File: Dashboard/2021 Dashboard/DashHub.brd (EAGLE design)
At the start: 86.4 x 66 mm, 26 parts, among them J1 LEFT, J2 RIGHT, U1 ALLEGRO_MICROSYSTEMS_ACS722LL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

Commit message: Linear Regulator
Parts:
- removed U$3: DC-DC-STEP-DOWN-MP1584, diy-modules:DC-DC-STEP-DOWN-MP1584
- added C3: 10uF, GTOR - Passive Components:C1206
- added C5, C6: 47uF, GTOR - Passive Components:C1206
- added U$6: TPSM84205EAB, GTOR - Active Components:TPSM84205EAB
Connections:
- removed net 3.3V_BUCK: J1.08, J2.08, U$3.OUT+.1, U$3.OUT+.2
- new net 3.3V_REG: C5.1, C6.1, J1.08, J2.08, U$6.3
- net 7.4V: now also C3.2, U$6.1; no longer U$3.IN+.1, U$3.IN+.2
- net GND: now also U$6.2; no longer U$3.IN-.1, U$3.IN-.2, U$3.OUT-.1, U$3.OUT-.2
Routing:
- net 3.3V_BUCK: track 75.9 -> 0.00 mm, vias 2 -> 0
- net 3.3V_REG: track 0.00 -> 68.9 mm, vias 0 -> 2
- net GND: track 336.4 -> 302.4 mm
- net 7.4V: track 158.7 -> 149.0 mm
- added copper zone on layer 1, net 3.3V_REG
- removed copper zone on layer 1, net 3.3V_BUCK
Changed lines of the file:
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@@
 <attribute name="VALUE" x="38.481" y="20.32" size="1.27" layer="27" rot="R90" align="top-center"/>
-</element>
-<element name="U$3" library="diy-modules" package="DC-DC-STEP-DOWN-MP1584" value="DC-DC-STEP-DOWN-MP1584" x="-33.02" y="-11.176" smashed="yes" rot="R90">
-<attribute name="NAME" x="-42.037" y="-11.176" size="1.27" layer="26" rot="MR270" align="bottom-center"/>
-<attribute name="VALUE" x="-23.495" y="-11.176" size="1.27" layer="27" rot="R90" align="top-center"/>
 </element>
 <element name="U$4" library="GTOR - Connectors" package="48CKTRASCMCHEADER" value="48CKTRASCMCHEADER" x="-10.16" y="23.368" smashed="yes" rot="MR0"/>
 <element name="U$5" library="GTOR - Breakout Boards" package="DIYMALL_6M_GPS_BREAKOUT" value="DIYMALL_6M_GPS_BREAKOUT" x="75.692" y="24.384" smashed="yes" rot="R179.9"/>
+<element name="U$6" library="GTOR - Active Components" package="TPSM84205EAB" value="TPSM84205EAB" x="-67.056" y="-27.94" smashed="yes">
+<attribute name="NAME" x="-72.136" y="-24.13" size="1.27" layer="25"/>
+<attribute name="VALUE" x="-72.136" y="-33.655" size="1.27" layer="27"/>
+</element>
+<element name="C3" library="GTOR - Passive Components" package="C1206" package3d_urn="urn:adsk.eagle:package:23618/2" value="10uF" x="-70.104" y="-42.164" smashed="yes">
+<attribute name="NAME" x="-71.374" y="-40.894" size="1.27" layer="25"/>
+<attribute name="POPULARITY" value="54" x="-70.104" y="-42.164" size="1.778" layer="27" display="off"/>
+<attribute name="SPICEPREFIX" value="C" x="-70.104" y="-42.164" size="1.778" layer="27" display="off"/>
+<attribute name="VALUE" x="-71.374" y="-44.704" size="1.27" layer="27"/>
+</element>
+<element name="C5" library="GTOR - Passive Components" package="C1206" package3d_urn="urn:adsk.eagle:package:23618/2" value="47uF" x="-70.104" y="-51.308" smashed="yes">
+<attribute name="NAME" x="-71.374" y="-50.038" size="1.27" layer="25"/>
+<attribute name="POPULARITY" value="54" x="-70.104" y="-51.308" size="1.778" layer="27" display="off"/>
+<attribute name="SPICEPREFIX" value="C" x="-70.104" y="-51.308" size="1.778" layer="27" display="off"/>
+<attribute name="VALUE" x="-71.374" y="-53.848" size="1.27" layer="27"/>
+</element>
+<element name="C6" library="GTOR - Passive Components" package="C1206" package3d_urn="urn:adsk.eagle:package:23618/2" value="47uF" x="-70.104" y="-55.88" smashed="yes">
+<attribute name="NAME" x="-71.374" y="-54.61" size="1.27" layer="25"/>
+<attribute name="POPULARITY" value="54" x="-70.104" y="-55.88" size="1.778" layer="27" display="off"/>
+<attribute name="SPICEPREFIX" value="C" x="-70.104" y="-55.88" size="1.778" layer="27" display="off"/>
+<attribute name="VALUE" x="-71.374" y="-58.42" size="1.27" layer="27"/>
+</element>
 </elements>
 <signals>
@@
 <contactref element="U$2" pad="OUT-.1"/>
 <contactref element="U$2" pad="OUT-.2"/>
-<contactref element="U$3" pad="IN-.1"/>
-<contactref element="U$3" pad="IN-.2"/>
-<contactref element="U$3" pad="OUT-.1"/>
-<contactref element="U$3" pad="OUT-.2"/>
-<wire x1="-37.084" y1="-20.447" x2="-33.655" y2="-23.876" width="0.4064" layer="1"/>
 <wire x1="-33.655" y1="-23.876" x2="-24.892" y2="-23.876" width="0.4064" layer="1"/>
 <wire x1="-24.892" y1="-23.876" x2="-17.4498" y2="-16.4338" width="0.4064" layer="1"/>
@@
 <wire x1="38.608" y1="-19.812" x2="37.0538" y2="-19.812" width="0.1524" layer="1"/>
 <wire x1="37.0538" y1="-19.812" x2="36.6794" y2="-19.4376" width="0.1524" layer="1"/>
-<wire x1="-37.084" y1="-20.447" x2="-39.624" y2="-20.447" width="0.1524" layer="1"/>
-<wire x1="-39.624" y1="-20.447" x2="-39.584" y2="-20.487" width="0.1524" layer="1"/>
 <wire x1="-39.584" y1="-20.487" x2="-39.584" y2="-27.813" width="0.1524" layer="1"/>
 <wire x1="-27.178" y1="-30.613" x2="-27.8944" y2="-29.8966" width="0.1524" layer="16"/>
@@
 <wire x1="-27.8944" y1="-29.6433125" x2="-28.3785125" y2="-29.1592" width="0.1524" layer="16"/>
 <wire x1="-28.3785125" y1="-29.1592" x2="-31.62225625" y2="-29.1592" width="0.1524" layer="16"/>
-<wire x1="-39.624" y1="-20.447" x2="-39.624" y2="-2.032" width="0.1524" layer="1"/>
-<wire x1="-39.624" y1="-2.032" x2="-39.624" y2="-1.905" width="0.1524" layer="1"/>
-<wire x1="-37.084" y1="-1.905" x2="-37.211" y2="-2.032" width="0.1524" layer="1"/>
-<wire x1="-37.211" y1="-2.032" x2="-39.624" y2="-2.032" width="0.1524" layer="1"/>
-<wire x1="-39.624" y1="-1.905" x2="-39.624" y2="3.556" width="0.1524" layer="16"/>
 <wire x1="-39.624" y1="3.556" x2="-35.56" y2="7.62" width="0.1524" layer="16"/>
 <wire x1="-35.56" y1="7.62" x2="-35.56" y2="9.525" width="0.1524" layer="16"/>
@@
 <wire x1="37.084" y1="0" x2="16.51" y2="0" width="0.1524" layer="1"/>
 <wire x1="11.43" y1="5.08" x2="16.51" y2="0" width="0.1524" layer="1"/>
-<wire x1="36.6794" y1="-19.4376" x2="74.16810625" y2="10.6966375" width="0" layer="19" extent="1-1"/>
+<contactref element="U$6" pad="2"/>
+<wire x1="-39.584" y1="-27.813" x2="-67.056" y2="-27.94" width="0" layer="19" extent="1-1"/>
+<wire x1="-33.655" y1="-23.876" x2="-39.584" y2="-20.487" width="0" layer="19" extent="1-1"/>
+<wire x1="-39.624" y1="3.556" x2="-39.584" y2="-20.487" width="0" layer="19" extent="1-16"/>
+<wire x1="74.16810625" y1="10.6966375" x2="36.6794" y2="-19.4376" width="0" layer="19" extent="1-1"/>
 </signal>
 <signal name="LAT_L">
@@
 <contactref element="U$2" pad="IN+.1"/>
 <contactref element="U$2" pad="IN+.2"/>
-<contactref element="U$3" pad="IN+.1"/>
-<contactref element="U$3" pad="IN+.2"/>
-<wire x1="-26.416" y1="-20.447" x2="-28.956" y2="-20.447" width="0.4064" layer="16"/>
-<wire x1="-26.416" y1="-20.447" x2="-22.733" y2="-16.764" width="0.4064" layer="1"/>
 <wire x1="-22.733" y1="-16.764" x2="-19.304" y2="-16.764" width="0.4064" layer="1"/>
 <wire x1="-19.304" y1="-16.764" x2="-18.796" y2="-16.256" width="0.4064" layer="1"/>
@@
 <wire x1="-28.448" y1="-25.013" x2="-28.448" y2="-22.86" width="0.4064" layer="16"/>
 <wire x1="-28.448" y1="-22.86" x2="-28.956" y2="-22.352" width="0.4064" layer="16"/>
-<wire x1="-28.956" y1="-22.352" x2="-28.956" y2="-20.447" width="0.4064" layer="16"/>
 <wire x1="39.116" y1="7.493" x2="35.56" y2="11.049" width="0.4064" layer="16"/>
 <wire x1="39.116" y1="-22.352" x2="39.116" y2="7.493" width="0.4064" layer="16"/>
 <wire x1="35.56" y1="11.049" x2="33.02" y2="11.049" width="0.4064" layer="16"/>
+<contactref element="U$6" pad="1"/>
+<contactref element="C3" pad="2"/>
+<wire x1="-69.596" y1="-27.94" x2="-68.704" y2="-42.164" width="0" layer="19" extent="1-1"/>
+<wire x1="-28.956" y1="-22.352" x2="-69.596" y2="-27.94" width="0" layer="19" extent="16-16"/>
+<wire x1="-27.178" y1="-25.013" x2="-28.448" y2="-25.013" width="0" layer="19" extent="16-16"/>
+<wire x1="-22.733" y1="-16.764" x2="-28.956" y2="-22.352" width="0" layer="19" extent="1-16"/>
 </signal>
 <signal name="3.3V_TEENSY">
@@
 <wire x1="6.1084" y1="19.812" x2="1.536" y2="19.812" width="0.1524" layer="16"/>
 </signal>
-<signal name="3.3V_BUCK">
+<signal name="3.3V_REG">
 <contactref element="J1" pad="08"/>
 <polygon width="0.1524" layer="1">
@@
 <wire x1="-21.59" y1="-11.43" x2="-19.57761875" y2="-11.43" width="0.4064" layer="16"/>
 <contactref element="J2" pad="08"/>
-<contactref element="U$3" pad="OUT+.1"/>
-<contactref element="U$3" pad="OUT+.2"/>
-<wire x1="-26.416" y1="-1.905" x2="-28.956" y2="-1.905" width="0.3048" layer="16"/>
 <wire x1="-21.971" y1="-5.842" x2="-25.908" y2="-1.905" width="0.4064" layer="16"/>
-<wire x1="-25.908" y1="-1.905" x2="-26.416" y2="-1.905" width="0.4064" layer="16"/>
 <wire x1="14.269075" y1="-4.4282" x2="13.904875" y2="-4.064" width="0.1524" layer="1"/>
 <wire x1="13.904875" y1="-4.064" x2="9.652" y2="-4.064" width="0.1524" layer="1"/>
@@
 <wire x1="-9.493" y1="0.508" x2="-9.775075" y2="0.508" width="0.1524" layer="16"/>
 <via x="-26.416" y="2.032" extent="1-16" drill="0.35"/>
-<wire x1="-26.416" y1="2.032" x2="-26.416" y2="-1.905" width="0.1524" layer="1"/>
+<contactref element="U$6" pad="3"/>
+<contactref element="C5" pad="1"/>
+<contactref element="C6" pad="1"/>
+<wire x1="-71.504" y1="-51.308" x2="-71.504" y2="-55.88" width="0" layer="19" extent="1-1"/>
+<wire x1="-64.516" y1="-27.94" x2="-71.504" y2="-51.308" width="0" layer="19" extent="1-1"/>
+<wire x1="-25.908" y1="-1.905" x2="-64.516" y2="-27.94" width="0" layer="19" extent="16-16"/>
+<wire x1="-26.416" y1="2.032" x2="-25.908" y2="-1.905" width="0" layer="19" extent="16-16"/>
 </signal>
 <signal name="LAT_D">

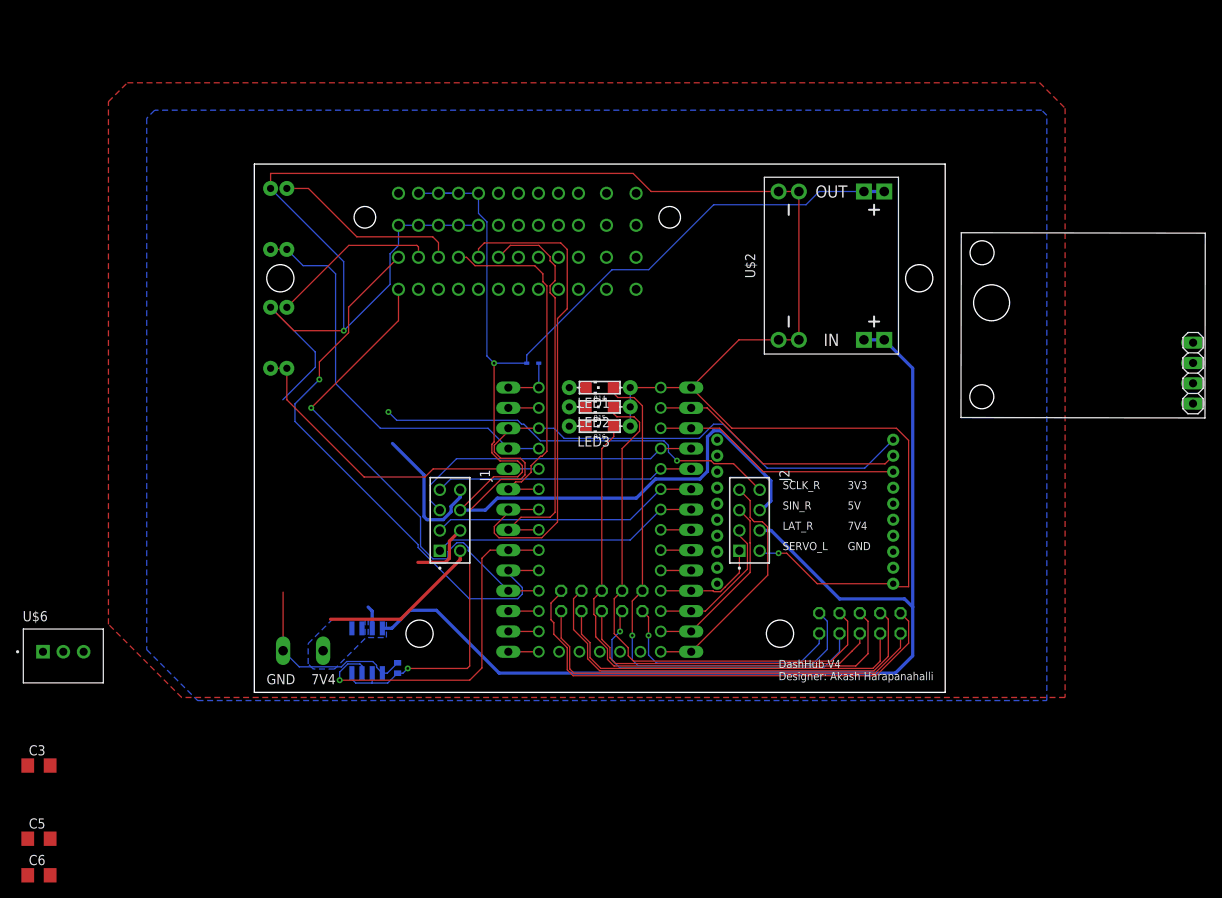
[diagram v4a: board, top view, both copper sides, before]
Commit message: Added new linear regulator and XBee silkscreen to dashhub
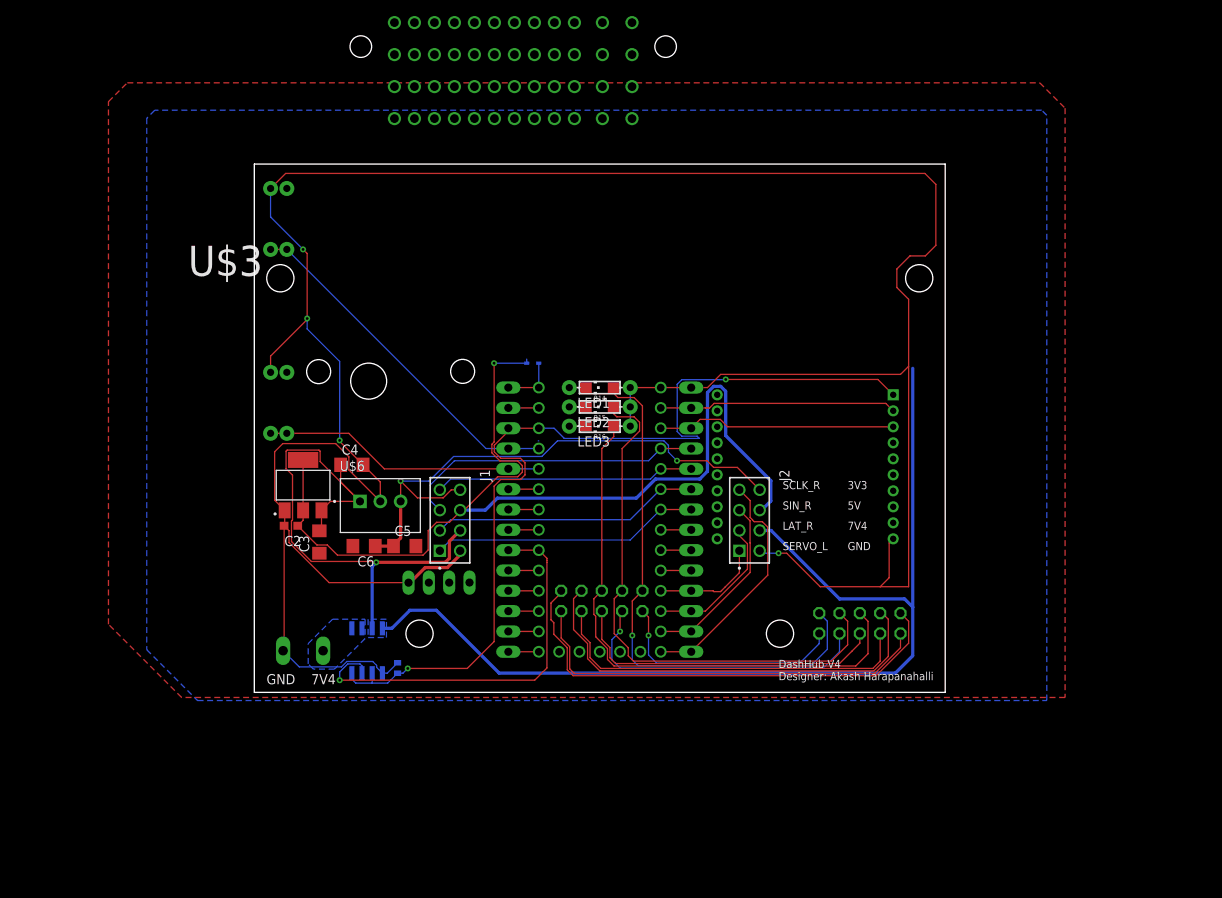
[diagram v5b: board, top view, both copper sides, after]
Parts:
- removed JP1: (no value), SparkFun-RF:XBEE
- removed U$2: DC-DC-STEP-DOWN-MP1584, diy-modules:DC-DC-STEP-DOWN-MP1584
- added C2: 4.7uF, GTOR - Passive Components:C0603
- added C4: 1uF, GTOR - Passive Components:C1206
- added U$3: REG_5V_LDL1117S50R, GTOR - Active Components:SOT230P700X180-4N
- added U2: XBEE_PRO_S3B, GTOR - Microcontroller:XBEE_PRO_S3B
- moved U$5 122.0 mm to (-37.6, -20.8), flipped to the bottom, turned to 89.9 degrees
- moved C5 58.6 mm to (-24.4, -14.7)
- moved C6 57.8 mm to (-29.5, -14.7), turned to 180 degrees
- moved C3 44.8 mm to (-35.1, -14.2), turned to 90 degrees
- moved U$6 43.9 mm to (-27.4, -9.14)
- moved U$4 21.3 mm to (-10.7, 44.7)
- moved R10 8.13 mm to (-39.1, 3.17)
- moved R12 8.13 mm to (-41.1, 3.17)
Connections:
- net 3.3V_TEENSY: now also U2.1; no longer JP1.1
- net 5V: now also C2.1, U$3.2, U$3.4; no longer U$2.OUT+.1, U$2.OUT+.2
- net 7.4V: now also C4.1, U$3.3; no longer U$2.IN+.1, U$2.IN+.2
- net GND: now also C2.2, C4.2, U$3.1, U2.10; no longer JP1.10, U$2.IN-.1, U$2.IN-.2, U$2.OUT-.1, U$2.OUT-.2
- net XBEE_RX: now also U2.2; no longer JP1.2
- net XBEE_TX: now also U2.3; no longer JP1.3
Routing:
- net AUX_TX: track 71.4 -> 3.81 mm, vias 1 -> 0
- net ANALOG2: track 63.8 -> 3.81 mm
- net AUX_RX: track 61.8 -> 3.81 mm, vias 1 -> 0
- net 7.4V: track 149.0 -> 201.8 mm, vias 0 -> 1
- net ANALOG3: track 50.9 -> 3.81 mm
- net GND: track 302.4 -> 347.6 mm, vias 2 -> 4
- net ANALOG1: track 44.9 -> 3.81 mm
- net 5V: track 169.1 -> 128.7 mm
- net N$24: track 23.6 -> 0.00 mm
- net N$23: track 21.0 -> 0.00 mm
- net 3.3V_TEENSY: track 108.7 -> 117.1 mm, vias 1 -> 2
- net SECONDARY_RPM: track 51.9 -> 43.8 mm
- net ENGINE_RPM: track 41.9 -> 35.4 mm
- net CURR_SENSE: track 44.9 -> 50.7 mm
- net XBEE_RX: track 32.4 -> 29.7 mm
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
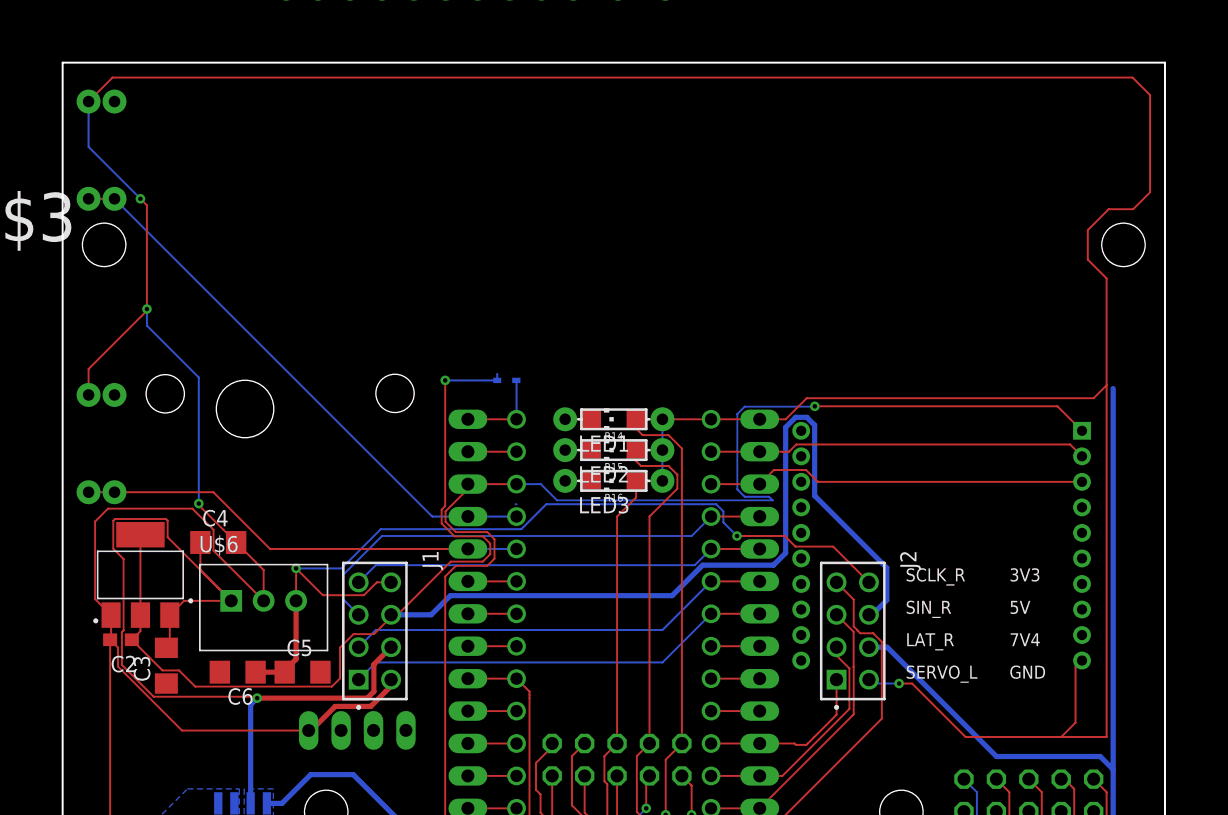
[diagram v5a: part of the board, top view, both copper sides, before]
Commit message: Moved stuff around to try and make space for the fat connect
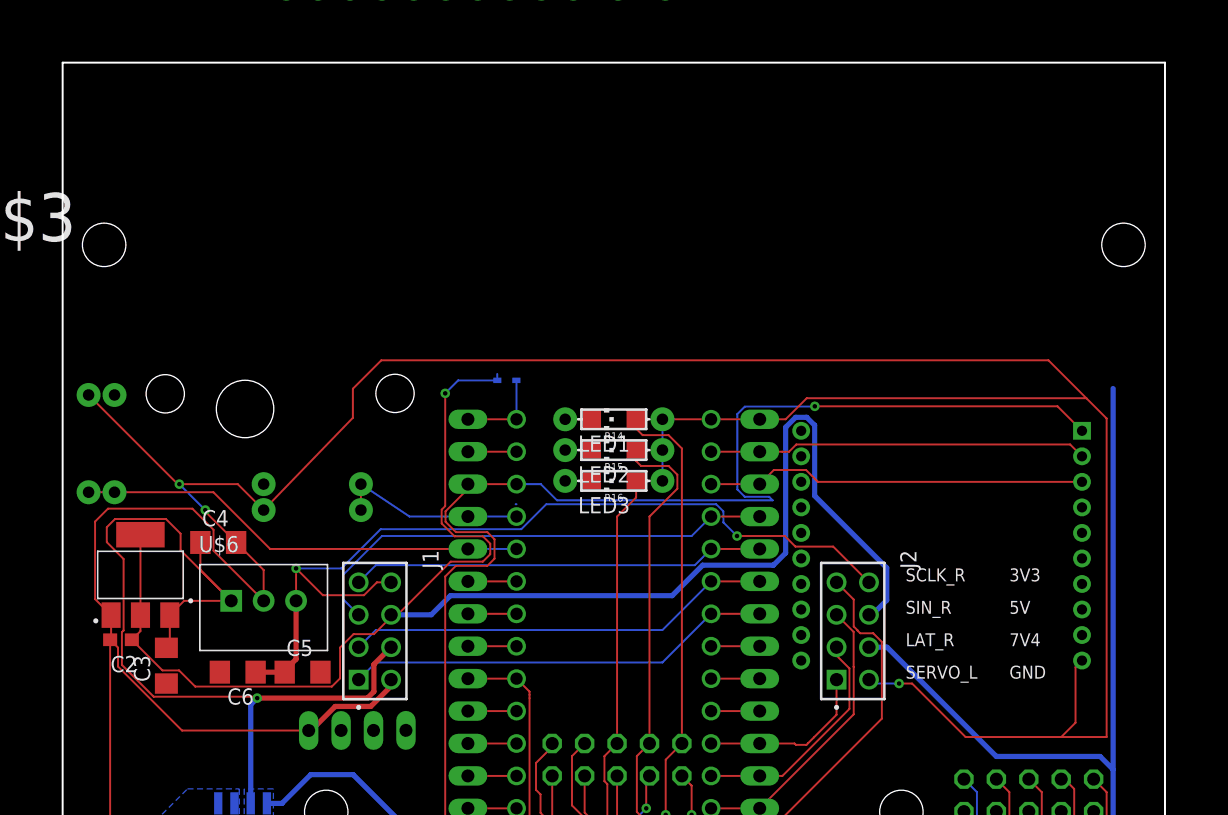
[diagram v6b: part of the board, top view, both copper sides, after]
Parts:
- moved R13 33.2 mm to (-23.6, -2.03), turned to 180 degrees
- moved R11 30.4 mm to (-23.6, 0.00), turned to 0 degrees
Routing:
- net GND: track 347.6 -> 282.1 mm, vias 4 -> 3
- net SECONDARY_RPM: track 43.8 -> 15.0 mm
- net 5V: track 128.7 -> 128.1 mm

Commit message: Added gps to dashhub
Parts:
- added U$2: OLED_SSD1306, GTOR - Breakout Boards:OLED_SSD1306
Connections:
- net 5V: now also U$2.VCC
- net GND: now also U$2.GND
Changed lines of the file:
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@@
 <attribute name="VALUE" x="11.4114" y="-17.5885" size="1.271609375" layer="28" rot="MR90"/>
+</element>
+<element name="U$2" library="GTOR - Breakout Boards" package="OLED_SSD1306" value="OLED_SSD1306" x="0" y="30.353" smashed="yes" rot="R270">
+<attribute name="NAME" x="12.9112" y="26.3868" size="1.27" layer="25" ratio="10" rot="R90"/>
 </element>
 </elements>
@@
 <wire x1="-34.036" y1="0" x2="-34.163" y2="0" width="0.1524" layer="1"/>
 <wire x1="-34.163" y1="0" x2="-41.148" y2="6.985" width="0.1524" layer="1"/>
+<contactref element="U$2" pad="GND"/>
+<wire x1="-23.904640625" y1="-19.304109375" x2="-23.904640625" y2="-19.30410625" width="0" layer="19" extent="1-1"/>
+<wire x1="-3.81" y1="30.353" x2="3.81" y2="5.08" width="0" layer="19" extent="1-1"/>
+<wire x1="-15.668" y1="46.704" x2="-3.81" y2="30.353" width="0" layer="19" extent="1-1"/>
 <wire x1="-18.168" y1="46.704" x2="-15.668" y2="46.704" width="0" layer="19" extent="1-1"/>
 <wire x1="-20.668" y1="46.704" x2="-18.168" y2="46.704" width="0" layer="19" extent="1-1"/>
 <wire x1="-23.168" y1="46.704" x2="-20.668" y2="46.704" width="0" layer="19" extent="1-1"/>
 <wire x1="-25.668" y1="46.704" x2="-23.168" y2="46.704" width="0" layer="19" extent="1-1"/>
-<wire x1="-41.148" y1="6.985" x2="-25.668" y2="46.704" width="0" layer="19" extent="1-1"/>
 </signal>
 <signal name="LAT_L">
@@
 <wire x1="15.735" y1="-0.91266875" x2="21.385" y2="-6.56266875" width="0.4064" layer="16"/>
 <wire x1="13.462" y1="-5.39053125" x2="13.462" y2="4.45345" width="0.4064" layer="16"/>
+<contactref element="U$2" pad="VCC"/>
 <wire x1="-18.168" y1="50.704" x2="-15.668" y2="50.704" width="0" layer="19" extent="1-1"/>
 <wire x1="-20.668" y1="50.704" x2="-18.168" y2="50.704" width="0" layer="19" extent="1-1"/>
 <wire x1="-23.168" y1="50.704" x2="-20.668" y2="50.704" width="0" layer="19" extent="1-1"/>
-<wire x1="-9.132" y1="8.636" x2="-15.668" y2="50.704" width="0" layer="19" extent="16-16"/>
+<wire x1="-1.27" y1="30.353" x2="-15.668" y2="50.704" width="0" layer="19" extent="1-1"/>
+<wire x1="-9.132" y1="8.636" x2="-1.27" y2="30.353" width="0" layer="19" extent="16-16"/>
 </signal>
 <signal name="3.3V_REG">
